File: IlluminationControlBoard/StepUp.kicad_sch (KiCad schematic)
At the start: 14 parts, among them U3 TPS55340PWPR

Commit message: SchematicUpdates
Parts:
- C1: footprint (none) -> Capacitor_SMD:C_0805_2012Metric; DigikeyPartNumber (none) -> 587-6025-1-ND
- C15: footprint (none) -> Capacitor_SMD:C_0603_1608Metric; DigikeyPartNumber (none) -> 311-4064-1-ND
- C2: footprint (none) -> Capacitor_SMD:C_0603_1608Metric; DigikeyPartNumber (none) -> 1276-1000-1-ND
- C3: footprint (none) -> Capacitor_SMD:C_0805_2012Metric; DigikeyPartNumber (none) -> 587-1438-1-ND
- C4: footprint (none) -> ATMARS_ILLUMINATION:CAP_PC_6P3X8_NCH; DigikeyPartNumber P16511CT-ND -> 493-13702-1-ND
- C6: footprint (none) -> Capacitor_SMD:C_0603_1608Metric; DigikeyPartNumber (none) -> 478-KGM15AR71C153KTCT-ND
- C7: footprint (none) -> Capacitor_SMD:C_0603_1608Metric; DigikeyPartNumber (none) -> 1276-2079-1-ND
- D1: footprint (none) -> Diode_SMD:D_SMC
- L1: footprint (none) -> Inductor_SMD:L_TDK_VLS6045EX_VLS6045AF
- R1: footprint (none) -> Resistor_SMD:R_0603_1608Metric; DigikeyPartNumber (none) -> 311-113KHRCT-ND
- R2: footprint (none) -> Resistor_SMD:R_0603_1608Metric; DigikeyPartNumber (none) -> RMCF0805FT60K4CT-ND
- R3: footprint (none) -> Resistor_SMD:R_0603_1608Metric; DigikeyPartNumber (none) -> P2.00KHCT-ND
- R4: footprint (none) -> Resistor_SMD:R_0603_1608Metric; DigikeyPartNumber (none) -> 311-10.0KHRCT-ND
- U3: DigikeyPartNumber (none) -> 296-39426-1-ND
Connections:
- net GND: now also C1.2, C2.2
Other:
- moved on the sheet: C1
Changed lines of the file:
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@@
+	)
+	(junction
+		(at 50.8 41.91)
+		(diameter 0)
+		(color 0 0 0 0)
 	)
 	(junction
@@
 	)
 	(junction
-		(at 52.07 41.91)
+		(at 59.69 60.96)
 		(diameter 0)
 		(color 0 0 0 0)
@@
 	(wire
 		(pts
+			(xy 59.69 60.96) (xy 59.69 66.04)
+		)
+		(stroke
+			(width 0)
+			(type default)
+		)
+	)
+	(wire
+		(pts
 			(xy 101.6 63.5) (xy 85.09 63.5)
 		)
@@
 	(wire
 		(pts
-			(xy 52.07 46.99) (xy 52.07 41.91)
+			(xy 50.8 46.99) (xy 50.8 41.91)
 		)
 		(stroke
@@
 	(wire
 		(pts
-			(xy 52.07 54.61) (xy 52.07 60.96)
-		)
-		(stroke
-			(width 0)
-			(type default)
-		)
-	)
-	(wire
-		(pts
-			(xy 52.07 60.96) (xy 68.58 60.96)
+			(xy 50.8 54.61) (xy 50.8 60.96)
+		)
+		(stroke
+			(width 0)
+			(type default)
+		)
+	)
+	(wire
+		(pts
+			(xy 50.8 60.96) (xy 59.69 60.96)
 		)
 		(stroke
@@
 	(wire
 		(pts
+			(xy 50.8 41.91) (xy 68.58 41.91)
+		)
+		(stroke
+			(width 0)
+			(type default)
+		)
+	)
+	(wire
+		(pts
 			(xy 186.69 97.79) (xy 186.69 95.25)
 		)
@@
 	(wire
 		(pts
-			(xy 46.99 41.91) (xy 52.07 41.91)
+			(xy 46.99 41.91) (xy 50.8 41.91)
 		)
 		(stroke
@@
 	(wire
 		(pts
+			(xy 59.69 60.96) (xy 68.58 60.96)
+		)
+		(stroke
+			(width 0)
+			(type default)
+		)
+	)
+	(wire
+		(pts
 			(xy 166.37 58.42) (xy 166.37 60.96)
 		)
@@
 		(pts
 			(xy 101.6 71.12) (xy 101.6 73.66)
-		)
-		(stroke
-			(width 0)
-			(type default)
-		)
-	)
-	(wire
-		(pts
-			(xy 52.07 41.91) (xy 68.58 41.91)
 		)
 		(stroke
@@
 			)
 		)
-		(property "Footprint" ""
+		(property "Footprint" "Inductor_SMD:L_TDK_VLS6045EX_VLS6045AF"
 			(at 93.98 41.91 0)
 			(effects
@@
 			)
 		)
-		(property "Footprint" ""
+		(property "Footprint" "Diode_SMD:D_SMC"
 			(at 118.11 41.91 0)
 			(effects
@@
 			)
 		)
-		(property "Footprint" ""
+		(property "Footprint" "Resistor_SMD:R_0603_1608Metric"
 			(at 192.278 50.8 90)
 			(effects
@@
 			)
 		)
-		(property "DigikeyPartNumber" ""
+		(property "DigikeyPartNumber" "311-113KHRCT-ND"
 			(at 190.5 50.8 0)
 			(effects
@@
 			)
 		)
-		(property "Footprint" ""
+		(property "Footprint" "ATMARS_ILLUMINATION:CAP_PC_6P3X8_NCH"
 			(at 203.2 50.8 0)
 			(effects
@@
 			)
 		)
-		(property "DigikeyPartNumber" "P16511CT-ND"
+		(property "DigikeyPartNumber" "493-13702-1-ND"
 			(at 203.2 50.8 0)
 			(effects
@@
 			)
 		)
-		(property "Footprint" ""
+		(property "Footprint" "Capacitor_SMD:C_0603_1608Metric"
 			(at 85.3948 73.66 0)
 			(effects
@@
 			)
 		)
-		(property "DigikeyPartNumber" ""
+		(property "DigikeyPartNumber" "1276-2079-1-ND"
 			(at 86.36 77.47 0)
 			(effects
@@
 			)
 		)
-		(property "Footprint" ""
+		(property "Footprint" "Resistor_SMD:R_0603_1608Metric"
 			(at 199.898 82.55 90)
 			(effects
@@
 			)
 		)
-		(property "DigikeyPartNumber" ""
+		(property "DigikeyPartNumber" "311-10.0KHRCT-ND"
 			(at 198.12 82.55 0)
 			(effects
@@
 			)
 		)
-		(property "DigikeyPartNumber" ""
+		(property "DigikeyPartNumber" "296-39426-1-ND"
 			(at 105.41 58.42 0)
 			(effects
@@
 	(symbol
 		(lib_id "Device:C")
-		(at 52.07 50.8 0)
+		(at 50.8 50.8 0)
 		(unit 1)
 		(exclude_from_sim no)
@@
 		(fields_autoplaced yes)
 		(property "Reference" "C1"
-			(at 54.991 49.5878 0)
+			(at 53.721 49.5878 0)
 			(effects
 				(font
@@
 		)
 		(property "Value" "10uF, 25V"
-			(at 54.991 52.0121 0)
+			(at 53.721 52.0121 0)
 			(effects
 				(font
@@
 			)
 		)
-		(property "Footprint" ""
-			(at 53.0352 54.61 0)
+		(property "Footprint" "Capacitor_SMD:C_0805_2012Metric"
+			(at 51.7652 54.61 0)
 			(effects
 				(font
@@
 		)
 		(property "Datasheet" "~"
-			(at 52.07 50.8 0)
+			(at 50.8 50.8 0)
 			(effects
 				(font
@@
 		)
 		(property "Description" "Unpolarized capacitor"
-			(at 52.07 50.8 0)
-			(effects
-				(font
-					(size 1.27 1.27)
-				)
-				(hide yes)
-			)
-		)
-		(property "DigikeyPartNumber" ""
-			(at 52.07 50.8 0)
+			(at 50.8 50.8 0)
+			(effects
+				(font
+					(size 1.27 1.27)
+				)
+				(hide yes)
+			)
+		)
+		(property "DigikeyPartNumber" "587-6025-1-ND"
+			(at 50.8 50.8 0)
 			(effects
 				(font
@@
 			)
 		)
-		(property "Footprint" ""
+		(property "Footprint" "Capacitor_SMD:C_0603_1608Metric"
 			(at 171.1452 92.71 0)
 			(effects
@@
 			)
 		)
-		(property "DigikeyPartNumber" ""
+		(property "DigikeyPartNumber" "311-4064-1-ND"
 			(at 170.18 88.9 0)
 			(effects
@@
 			)
 		)
-		(property "Footprint" ""
+		(property "Footprint" "Resistor_SMD:R_0603_1608Metric"
 			(at 177.8 81.788 90)
 			(effects
@@
 			)
 		)
-		(property "DigikeyPartNumber" ""
+		(property "DigikeyPartNumber" "P2.00KHCT-ND"
 			(at 177.8 80.01 0)
 			(effects
@@
 				(path "/475a05fd-52d9-442f-b4d1-e854012dfab2/c3028b56-f565-42f5-ab14-a6a5b2effaaf"
 					(reference "R3")
+					(unit 1)
+				)
+			)
+		)
+	)
+	(symbol
+		(lib_id "power:GND")
+		(at 59.69 66.04 0)
+		(unit 1)
+		(exclude_from_sim no)
+		(in_bom yes)
+		(on_board yes)
+		(dnp no)
+		(fields_autoplaced yes)
+		(property "Reference" "#PWR010"
+			(at 59.69 72.39 0)
+			(effects
+				(font
+					(size 1.27 1.27)
+				)
+				(hide yes)
+			)
+		)
+		(property "Value" "GND"
+			(at 59.69 70.1731 0)
+			(effects
+				(font
+					(size 1.27 1.27)
+				)
+			)
+		)
+		(property "Footprint" ""
+			(at 59.69 66.04 0)
+			(effects
+				(font
+					(size 1.27 1.27)
+				)
+				(hide yes)
+			)
+		)
+		(property "Datasheet" ""
+			(at 59.69 66.04 0)
+			(effects
+				(font
+					(size 1.27 1.27)
+				)
+				(hide yes)
+			)
+		)
+		(property "Description" "Power symbol creates a global label with name \"GND\" , ground"
+			(at 59.69 66.04 0)
+			(effects
+				(font
+					(size 1.27 1.27)
+				)
+				(hide yes)
+			)
+		)
+		(pin "1"
+		)
+		(instances
+			(project "IlluminationControlBoard"
+				(path "/475a05fd-52d9-442f-b4d1-e854012dfab2/c3028b56-f565-42f5-ab14-a6a5b2effaaf"
+					(reference "#PWR010")
 					(unit 1)
 				)
@@
 			)
 		)
-		(property "Footprint" ""
+		(property "Footprint" "Resistor_SMD:R_0603_1608Metric"
 			(at 177.8 72.898 90)
 			(effects
@@
 			)
 		)
-		(property "DigikeyPartNumber" ""
+		(property "DigikeyPartNumber" "RMCF0805FT60K4CT-ND"
 			(at 177.8 71.12 0)
 			(effects
@@
 			)
 		)
-		(property "Footprint" ""
+		(property "Footprint" "Capacitor_SMD:C_0603_1608Metric"
 			(at 69.5452 54.61 0)
 			(effects
@@
 			)
 		)
-		(property "DigikeyPartNumber" ""
+		(property "DigikeyPartNumber" "1276-1000-1-ND"
 			(at 68.58 50.8 0)
 			(effects
@@
 			)
 		)
-		(property "Footprint" ""
+		(property "Footprint" "Capacitor_SMD:C_0805_2012Metric"
 			(at 214.9348 46.99 0)
 			(effects
@@
 			)
 		)
-		(property "DigikeyPartNumber" ""
+		(property "DigikeyPartNumber" "587-1438-1-ND"
 			(at 215.9 50.8 0)
 			(effects
@@
 			)
 		)
-		(property "Footprint" ""
+		(property "Footprint" "Capacitor_SMD:C_0603_1608Metric"
 			(at 187.6552 92.71 0)
 			(effects
@@
 			)
 		)
-		(property "DigikeyPartNumber" ""
+		(property "DigikeyPartNumber" "478-KGM15AR71C153KTCT-ND"
 			(at 186.69 88.9 0)
 			(effects

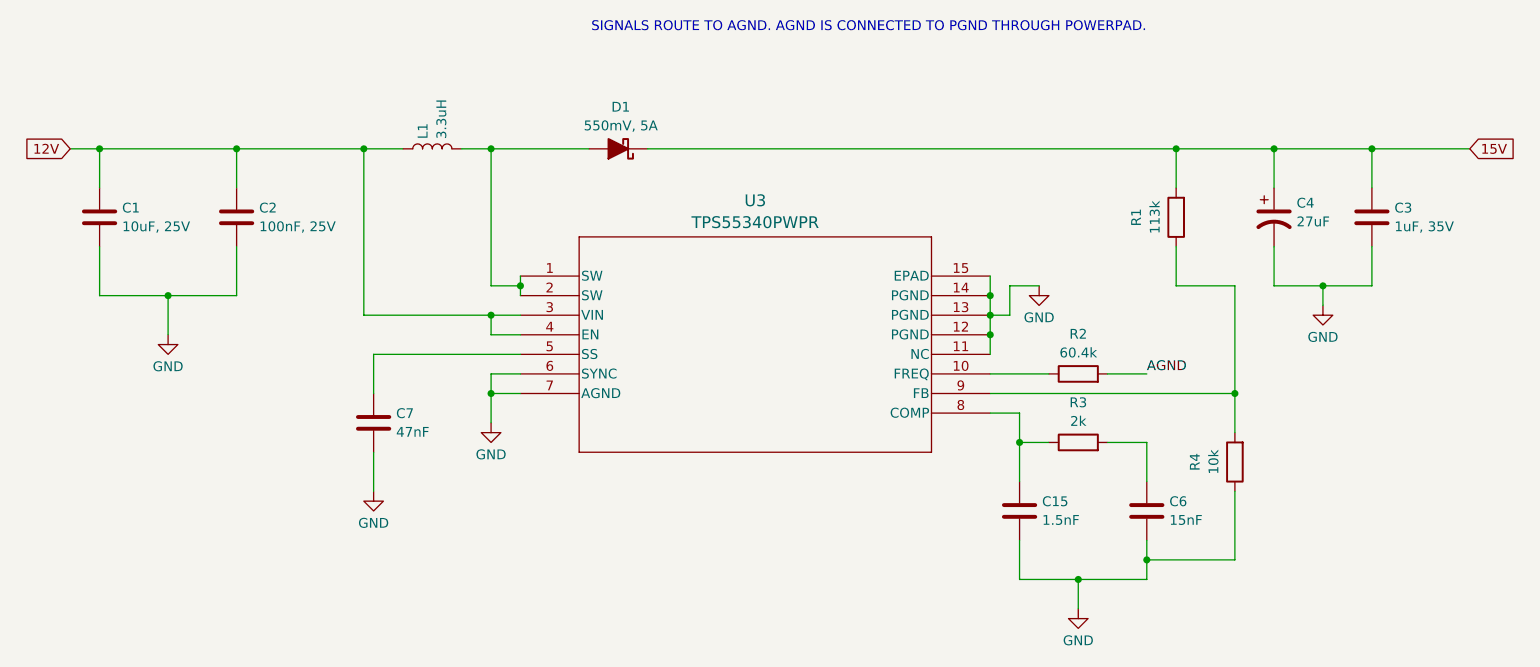
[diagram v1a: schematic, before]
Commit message: PCB designed
Designed and populated PCB to provide 15V to illumination.
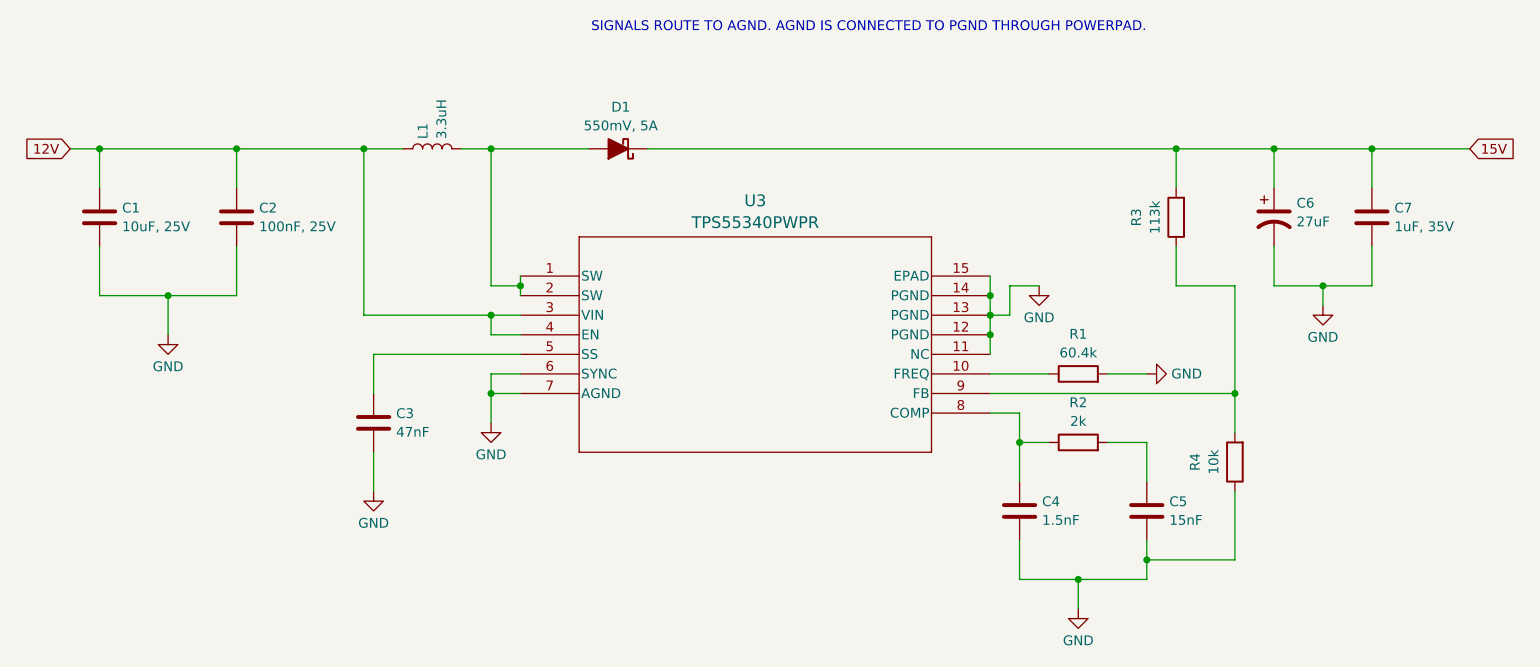
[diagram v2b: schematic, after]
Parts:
- renumbered C7 to C3, C15 to C4, C6 to C5, C4 to C6, C3 to C7, R2 to R1, R3 to R2, R1 to R3
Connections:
- net AGND is gone; now on net GND: R1.2
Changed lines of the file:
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@@
 		)
 	)
-	(label "AGND"
-		(at 186.69 71.12 0)
+	(global_label "15V"
+		(shape input)
+		(at 228.6 41.91 0)
 		(fields_autoplaced yes)
 		(effects
@@
 				(size 1.27 1.27)
 			)
-			(justify left bottom)
-		)
-	)
-	(global_label "15V"
+			(justify left)
+		)
+		(property "Intersheetrefs" "${INTERSHEET_REFS}"
+			(at 235.0928 41.91 0)
+			(effects
+				(font
+					(size 1.27 1.27)
+				)
+				(justify left)
+				(hide yes)
+			)
+		)
+	)
+	(global_label "12V"
 		(shape input)
-		(at 228.6 41.91 0)
+		(at 46.99 41.91 180)
 		(fields_autoplaced yes)
 		(effects
@@
 				(size 1.27 1.27)
 			)
-			(justify left)
-		)
-		(property "Intersheetrefs" "${INTERSHEET_REFS}"
-			(at 235.0928 41.91 0)
-			(effects
-				(font
-					(size 1.27 1.27)
-				)
-				(justify left)
-				(hide yes)
-			)
-		)
-	)
-	(global_label "12V"
-		(shape input)
-		(at 46.99 41.91 180)
-		(fields_autoplaced yes)
-		(effects
-			(font
-				(size 1.27 1.27)
-			)
 			(justify right)
 		)
@@
 		(dnp no)
 		(fields_autoplaced yes)
-		(property "Reference" "#PWR09"
+		(property "Reference" "#PWR08"
 			(at 101.6 83.82 0)
 			(effects
@@
 			(project "IlluminationControlBoard"
 				(path "/475a05fd-52d9-442f-b4d1-e854012dfab2/c3028b56-f565-42f5-ab14-a6a5b2effaaf"
-					(reference "#PWR09")
+					(reference "#PWR08")
 					(unit 1)
 				)
@@
 		(dnp no)
 		(fields_autoplaced yes)
-		(property "Reference" "#PWR07"
+		(property "Reference" "#PWR010"
 			(at 177.8 107.95 0)
 			(effects
@@
 			(project "IlluminationControlBoard"
 				(path "/475a05fd-52d9-442f-b4d1-e854012dfab2/c3028b56-f565-42f5-ab14-a6a5b2effaaf"
-					(reference "#PWR07")
+					(reference "#PWR010")
 					(unit 1)
 				)
@@
 		(on_board yes)
 		(dnp no)
-		(property "Reference" "R1"
+		(property "Reference" "R3"
 			(at 185.3395 50.8 90)
 			(effects
@@
 			(project ""
 				(path "/475a05fd-52d9-442f-b4d1-e854012dfab2/c3028b56-f565-42f5-ab14-a6a5b2effaaf"
-					(reference "R1")
+					(reference "R3")
 					(unit 1)
 				)
@@
 		(dnp no)
 		(fields_autoplaced yes)
-		(property "Reference" "C4"
+		(property "Reference" "C6"
 			(at 206.121 48.9528 0)
 			(effects
@@
 			(project ""
 				(path "/475a05fd-52d9-442f-b4d1-e854012dfab2/c3028b56-f565-42f5-ab14-a6a5b2effaaf"
-					(reference "C4")
+					(reference "C6")
 					(unit 1)
 				)
@@
 		(dnp no)
 		(fields_autoplaced yes)
-		(property "Reference" "C7"
+		(property "Reference" "C3"
 			(at 89.281 76.2578 0)
 			(effects
@@
 			(project "IlluminationControlBoard"
 				(path "/475a05fd-52d9-442f-b4d1-e854012dfab2/c3028b56-f565-42f5-ab14-a6a5b2effaaf"
-					(reference "C7")
+					(reference "C3")
 					(unit 1)
 				)
@@
 		)
 		(property "DigikeyPartNumber" "296-39426-1-ND"
-			(at 105.41 58.42 0)
+			(at 104.648 54.864 0)
 			(effects
 				(font
@@
 		(dnp no)
 		(fields_autoplaced yes)
-		(property "Reference" "#PWR08"
+		(property "Reference" "#PWR07"
 			(at 86.36 92.71 0)
 			(effects
@@
 			(project "IlluminationControlBoard"
 				(path "/475a05fd-52d9-442f-b4d1-e854012dfab2/c3028b56-f565-42f5-ab14-a6a5b2effaaf"
-					(reference "#PWR08")
+					(reference "#PWR07")
 					(unit 1)
 				)
@@
 		(dnp no)
 		(fields_autoplaced yes)
-		(property "Reference" "#PWR06"
+		(property "Reference" "#PWR012"
 			(at 209.55 68.58 0)
 			(effects
@@
 			(project "IlluminationControlBoard"
 				(path "/475a05fd-52d9-442f-b4d1-e854012dfab2/c3028b56-f565-42f5-ab14-a6a5b2effaaf"
-					(reference "#PWR06")
+					(reference "#PWR012")
 					(unit 1)
 				)
@@
 		(dnp no)
 		(fields_autoplaced yes)
-		(property "Reference" "C15"
+		(property "Reference" "C4"
 			(at 173.101 87.6878 0)
 			(effects
@@
 			(project "IlluminationControlBoard"
 				(path "/475a05fd-52d9-442f-b4d1-e854012dfab2/c3028b56-f565-42f5-ab14-a6a5b2effaaf"
-					(reference "C15")
+					(reference "C4")
+					(unit 1)
+				)
+			)
+		)
+	)
+	(symbol
+		(lib_id "power:GND")
+		(at 186.69 71.12 90)
+		(unit 1)
+		(exclude_from_sim no)
+		(in_bom yes)
+		(on_board yes)
+		(dnp no)
+		(fields_autoplaced yes)
+		(property "Reference" "#PWR011"
+			(at 193.04 71.12 0)
+			(effects
+				(font
+					(size 1.27 1.27)
+				)
+				(hide yes)
+			)
+		)
+		(property "Value" "GND"
+			(at 189.865 71.12 90)
+			(effects
+				(font
+					(size 1.27 1.27)
+				)
+				(justify right)
+			)
+		)
+		(property "Footprint" ""
+			(at 186.69 71.12 0)
+			(effects
+				(font
+					(size 1.27 1.27)
+				)
+				(hide yes)
+			)
+		)
+		(property "Datasheet" ""
+			(at 186.69 71.12 0)
+			(effects
+				(font
+					(size 1.27 1.27)
+				)
+				(hide yes)
+			)
+		)
+		(property "Description" "Power symbol creates a global label with name \"GND\" , ground"
+			(at 186.69 71.12 0)
+			(effects
+				(font
+					(size 1.27 1.27)
+				)
+				(hide yes)
+			)
+		)
+		(pin "1"
+		)
+		(instances
+			(project "IlluminationControlBoard"
+				(path "/475a05fd-52d9-442f-b4d1-e854012dfab2/c3028b56-f565-42f5-ab14-a6a5b2effaaf"
+					(reference "#PWR011")
 					(unit 1)
 				)
@@
 		(dnp no)
 		(fields_autoplaced yes)
-		(property "Reference" "R3"
+		(property "Reference" "R2"
 			(at 177.8 74.8495 90)
 			(effects
@@
 			(project "IlluminationControlBoard"
 				(path "/475a05fd-52d9-442f-b4d1-e854012dfab2/c3028b56-f565-42f5-ab14-a6a5b2effaaf"
-					(reference "R3")
+					(reference "R2")
 					(unit 1)
 				)
@@
 		(dnp no)
 		(fields_autoplaced yes)
-		(property "Reference" "#PWR010"
+		(property "Reference" "#PWR06"
 			(at 59.69 72.39 0)
 			(effects
@@
 			(project "IlluminationControlBoard"
 				(path "/475a05fd-52d9-442f-b4d1-e854012dfab2/c3028b56-f565-42f5-ab14-a6a5b2effaaf"
-					(reference "#PWR010")
+					(reference "#PWR06")
 					(unit 1)
 				)
@@
 		(dnp no)
 		(fields_autoplaced yes)
-		(property "Reference" "R2"
+		(property "Reference" "R1"
 			(at 177.8 65.9595 90)
 			(effects
@@
 			(project ""
 				(path "/475a05fd-52d9-442f-b4d1-e854012dfab2/c3028b56-f565-42f5-ab14-a6a5b2effaaf"
-					(reference "R2")
+					(reference "R1")
 					(unit 1)
 				)
@@
 		(dnp no)
 		(fields_autoplaced yes)
-		(property "Reference" "#PWR05"
+		(property "Reference" "#PWR09"
 			(at 172.72 66.04 0)
 			(effects
@@
 			(project ""
 				(path "/475a05fd-52d9-442f-b4d1-e854012dfab2/c3028b56-f565-42f5-ab14-a6a5b2effaaf"
-					(reference "#PWR05")
+					(reference "#PWR09")
 					(unit 1)
 				)
@@
 		(dnp no)
 		(fields_autoplaced yes)
-		(property "Reference" "C3"
+		(property "Reference" "C7"
 			(at 218.821 49.5878 0)
 			(effects
@@
 			(project "IlluminationControlBoard"
 				(path "/475a05fd-52d9-442f-b4d1-e854012dfab2/c3028b56-f565-42f5-ab14-a6a5b2effaaf"
-					(reference "C3")
+					(reference "C7")
 					(unit 1)
 				)
@@
 		(dnp no)
 		(fields_autoplaced yes)
-		(property "Reference" "C6"
+		(property "Reference" "C5"
 			(at 189.611 87.6878 0)
 			(effects
@@
 			(project "IlluminationControlBoard"
 				(path "/475a05fd-52d9-442f-b4d1-e854012dfab2/c3028b56-f565-42f5-ab14-a6a5b2effaaf"
-					(reference "C6")
-					(unit 1)
-				)
+					(reference "C5")
+					(unit 1)
+				)
